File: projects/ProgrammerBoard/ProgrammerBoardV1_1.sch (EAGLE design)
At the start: 14 parts, among them J1 EQUISAT-UMBILICAL-CONN, J9 M50-3600542

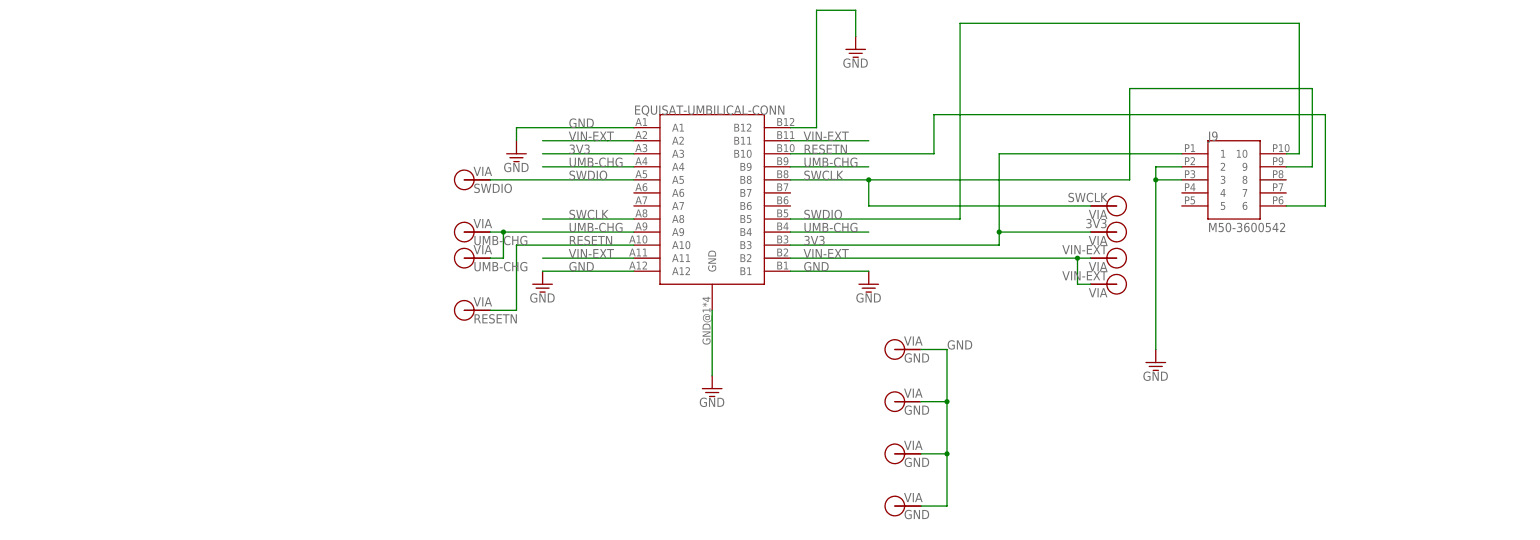
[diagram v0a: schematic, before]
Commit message: Updates to programmer board with correct connector, addition of TVS diodes, modified layout, and updated silkscreen.
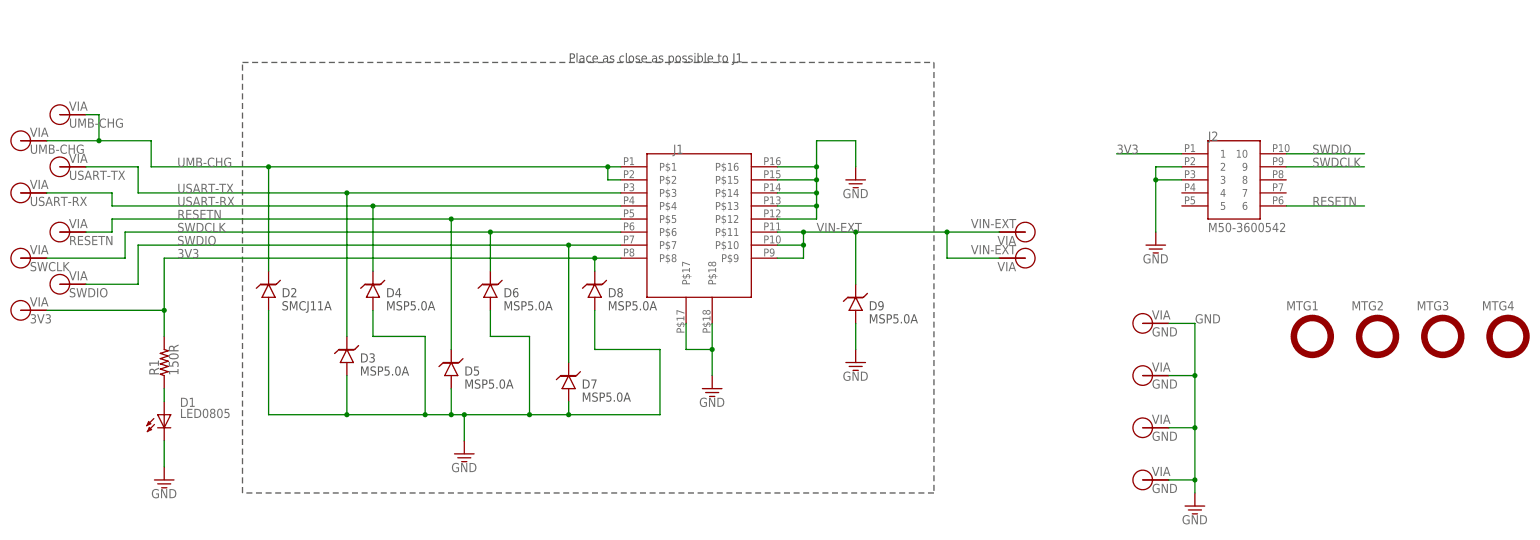
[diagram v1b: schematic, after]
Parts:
- added D1: LED0805, BrownSpaceEngineering:LED0805
- added D2: SMCJ11A, BrownSpaceEngineering:TVSSMCJ11A
- added D3, D4, D5, D6, D7, D8, D9: MSP5.0A, BrownSpaceEngineering:TVSMSP
- added MTG1, MTG2, MTG3, MTG4: (no value), BrownSpaceEngineering:MTG-NPTH-M2
- added R1: 150R, BrownSpaceEngineering:RES0805
- added V13: USART-RX, BrownSpaceEngineering:VIA-60MIL
- added V14: USART-TX, BrownSpaceEngineering:VIA-60MIL
- J1: value EQUISAT-UMBILICAL-CONN -> FFC-16REVERSE; device BrownSpaceEngineering:EQUISAT-UMBILICAL-CONN -> BrownSpaceEngineering:FFC-16REVERSE
- renumbered J9 to J2
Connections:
- removed net SWCLK: J1.A8, J1.B8, J2.9, V9.P$1
- new net N$2: D1.A, R1.1
- new net SWDCLK: D6.C, J1.P$6, J2.9, V9.P$1
- new net USART-RX: D4.C, J1.P$4, V13.P$1
- new net USART-TX: D3.C, J1.P$3, V14.P$1
- net 3V3: now also D8.C, J1.P$8, R1.2; no longer J1.A3, J1.B3
- net GND: now also D1.C, D2.A, D3.A, D4.A, D5.A, D6.A, D7.A, D8.A, D9.A, J1.P$12, J1.P$13, J1.P$14, J1.P$15, J1.P$16, J1.P$17, J1.P$18; no longer J1.A1, J1.A12, J1.B1, J1.B12, J1.GND
- net RESETN: now also D5.C, J1.P$5; no longer J1.A10, J1.B10
- net SWDIO: now also D7.C, J1.P$7; no longer J1.A5, J1.B5
- net UMB-CHG: now also D2.C, J1.P$1, J1.P$2; no longer J1.A4, J1.A9, J1.B4, J1.B9
- net VIN-EXT: now also D9.C, J1.P$10, J1.P$11, J1.P$9; no longer J1.A11, J1.A2, J1.B11, J1.B2
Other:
- note added: "Place as close as possible to J1"
